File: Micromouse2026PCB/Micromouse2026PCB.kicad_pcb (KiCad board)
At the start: 2 copper layers, 12 parts, among them J1 Power Terminal, U6 L7805

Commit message: New PCB work
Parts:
- added J2: i2c OLED, Connector_PinHeader_2.54mm:PinHeader_1x04_P2.54mm_Vertical, F.Cu at (83.8, 54.0)
- added J3: BNO085, Connector_PinHeader_2.54mm:PinHeader_1x06_P2.54mm_Vertical, F.Cu at (83.8, 34.9)
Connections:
- A1 pad A4: unconnected-(A1-PadA4) -> Net-(M1-OB)
- A1 pad A5: unconnected-(A1-PadA5) -> Net-(M2-OB)
- A1 pad D0: unconnected-(A1-D0/RX-PadD0) -> Net-(A1-D0/RX)
- A1 pad D1: unconnected-(A1-D1/TX-PadD1) -> Net-(A1-D1/TX)
- A1 pad D10: unconnected-(A1-PadD10) -> Net-(MD2-OB)
- A1 pad D5: unconnected-(A1-PadD5) -> Net-(MD1-OA)
- A1 pad D6: unconnected-(A1-PadD6) -> Net-(MD1-OB)
- A1 pad D9: unconnected-(A1-PadD9) -> Net-(MD2-OA)
- M1 pad 1: unconnected-(M1-MA-Pad1) -> Net-(M1-MA)
- M1 pad 2: unconnected-(M1-MB-Pad2) -> Net-(M1-MB)
- M1 pad 3: unconnected-(M1-VCC-Pad3) -> +5V
- M1 pad 4: unconnected-(M1-GND-Pad4) -> GND
- M1 pad 5: unconnected-(M1-OA-Pad5) -> Net-(A1-D1/TX)
- M1 pad 6: unconnected-(M1-OB-Pad6) -> Net-(M1-OB)
- M2 pad 1: unconnected-(M2-MA-Pad1) -> Net-(M2-MA)
- M2 pad 2: unconnected-(M2-MB-Pad2) -> Net-(M2-MB)
- M2 pad 3: unconnected-(M2-VCC-Pad3) -> +5V
- M2 pad 4: unconnected-(M2-GND-Pad4) -> GND
- M2 pad 5: unconnected-(M2-OA-Pad5) -> Net-(A1-D0/RX)
- M2 pad 6: unconnected-(M2-OB-Pad6) -> Net-(M2-OB)
- MD1 pad 1: unconnected-(MD1-OA-Pad1) -> Net-(MD1-OA)
- MD1 pad 4: unconnected-(MD1-OB-Pad4) -> Net-(MD1-OB)
- MD1 pad 6: unconnected-(MD1-IA-Pad6) -> Net-(M1-MA)
- MD1 pad 7: unconnected-(MD1-IB-Pad7) -> Net-(M1-MB)
- MD2 pad 1: unconnected-(MD2-OA-Pad1) -> Net-(MD2-OA)
- MD2 pad 4: unconnected-(MD2-OB-Pad4) -> Net-(MD2-OB)
- MD2 pad 6: unconnected-(MD2-IA-Pad6) -> Net-(M2-MA)
- MD2 pad 7: unconnected-(MD2-IB-Pad7) -> Net-(M2-MB)
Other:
- board outline added: 87 x 48.9 mm

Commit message: finished schematic
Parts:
- added SW1: RotaryEncoder_Switch, Rotary_Encoder:RotaryEncoder_Alps_EC11E-Switch_Vertical_H20mm, F.Cu at (90.4, 39.5)
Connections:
- A1 pad D10: Net-(MD2-OB) -> Net-(MD2-IB)
- A1 pad D4: unconnected-(A1-PadD4) -> Net-(A1-PadD4)
- A1 pad D5: Net-(MD1-OA) -> Net-(MD1-IA)
- A1 pad D6: Net-(MD1-OB) -> Net-(MD1-IB)
- A1 pad D7: unconnected-(A1-D7_INT4-PadD7) -> Net-(A1-D7_INT4)
- A1 pad D8: unconnected-(A1-PadD8) -> Net-(A1-PadD8)
- A1 pad D9: Net-(MD2-OA) -> Net-(MD2-IA)
- MD1 pad 1: Net-(MD1-OA) -> Net-(M1-MA)
- MD1 pad 4: Net-(MD1-OB) -> Net-(M1-MB)
- MD1 pad 6: Net-(M1-MA) -> Net-(MD1-IA)
- MD1 pad 7: Net-(M1-MB) -> Net-(MD1-IB)
- MD2 pad 1: Net-(MD2-OA) -> Net-(M2-MA)
- MD2 pad 4: Net-(MD2-OB) -> Net-(M2-MB)
- MD2 pad 6: Net-(M2-MA) -> Net-(MD2-IA)
- MD2 pad 7: Net-(M2-MB) -> Net-(MD2-IB)
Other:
- board outline removed

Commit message: PCB work
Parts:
- J2: footprint Connector_PinHeader_2.54mm:PinHeader_1x04_P2.54mm_Vertical -> CustomFootprints:OLED_0.96_SSD1306_I2C
- J3: footprint Connector_PinHeader_2.54mm:PinHeader_1x06_P2.54mm_Vertical -> CustomFootprints:Adafruit_BNO085
- moved J3 54.1 mm to (137.2, 43.8)
- moved J2 42.1 mm to (125.7, 58.4)
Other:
- board outline added: 24.9 x 25.5 mm

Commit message: PCB working version
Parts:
- removed U6: L7805, Package_TO_SOT_THT:TO-220-3_Vertical
- added D1: 1N5822, Diode_THT:D_DO-201AD_P15.24mm_Horizontal, F.Cu at (123.2, 88.3)
- added R1: 10k, Resistor_THT:R_Axial_DIN0207_L6.3mm_D2.5mm_P10.16mm_Horizontal, F.Cu at (100.1, 87.6)
- added R2: 10k, Resistor_THT:R_Axial_DIN0207_L6.3mm_D2.5mm_P10.16mm_Horizontal, F.Cu at (104.1, 87.6)
- added SW1: PowerSW, Connector_PinHeader_2.54mm:PinHeader_1x03_P2.54mm_Vertical, F.Cu at (118.7, 81.3)
- J1: footprint TerminalBlock_Phoenix:TerminalBlock_Phoenix_MKDS-1,5-2-5.08_1x02_P5.08mm_Horizontal -> TerminalBlock_Phoenix:TerminalBlock_Phoenix_MPT-0,5-2-2.54_1x02_P2.54mm_Horizontal
- moved J3 94.1 mm to (43.2, 48.3), turned to 180 degrees
- moved J1 80.2 mm to (102.9, 71.1), turned to 180 degrees
- moved A1 49.2 mm to (70.0, 81.4), turned to 90 degrees
- moved M2 38.0 mm to (48.3, 35.6), turned to -90 degrees
- moved RS1 33.0 mm to (109.3, 66.6)
- moved J2 31.4 mm to (99.1, 41.9), turned to 90 degrees
- moved U1 29.9 mm to (30.5, 83.8), turned to 90 degrees
- moved MD2 29.6 mm to (43.2, 43.2), turned to 180 degrees
- moved MD1 28.8 mm to (35.6, 71.1)
- moved U4 27.3 mm to (29.3, 36.7), turned to -45 degrees
- moved U5 26.6 mm to (43.2, 30.5), turned to -90 degrees
- moved U3 25.4 mm to (20.3, 50.8)
- moved U2 24.9 mm to (20.3, 68.6), turned to 45 degrees
- moved M1 12.1 mm to (48.3, 71.1), turned to -90 degrees
- renumbered SW1 to RS1
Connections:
- A1 pad A4: Net-(M1-OB) -> unconnected-(A1-PadA4)
- A1 pad A5: Net-(M2-OB) -> Net-(A1-PadA5)
- A1 pad D11: unconnected-(A1-PadD11) -> Net-(M2-OB)
- A1 pad D12: unconnected-(A1-PadD12) -> Net-(M1-OB)
- A1 pad VIN: Net-(J1-Pin_1) -> Net-(SW1-Pin_1)
- J1 pad 1: Net-(J1-Pin_1) -> Net-(D1-A)
- MD1 pad 2: Net-(U6-OUT) -> Net-(SW1-Pin_1)
- MD1 pad 3: Net-(U6-OUT) -> Net-(SW1-Pin_1)
- MD2 pad 2: Net-(U6-OUT) -> Net-(SW1-Pin_1)
- MD2 pad 3: Net-(U6-OUT) -> Net-(SW1-Pin_1)
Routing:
- net GND: track 0.00 -> 513.9 mm
- net +5V: track 0.00 -> 313.3 mm
- net Net-(SW1-Pin_1): track 0.00 -> 271.6 mm
- net /SDA: track 0.00 -> 255.9 mm
- net /SCL: track 0.00 -> 243.8 mm
- net Net-(MD2-IB): track 0.00 -> 127.7 mm
- net Net-(A1-PadA5): track 0.00 -> 112.7 mm
- net Net-(A1-PadD4): track 0.00 -> 88.3 mm
- net Net-(M2-OB): track 0.00 -> 82.6 mm
- net Net-(U4-XSHUT): track 0.00 -> 79.7 mm, vias 0 -> 1
- net Net-(A1-PadD8): track 0.00 -> 73.1 mm
- net Net-(A1-D7_INT4): track 0.00 -> 69.8 mm
- net Net-(U3-XSHUT): track 0.00 -> 66.0 mm, vias 0 -> 1
- net Net-(MD2-IA): track 0.00 -> 62.9 mm
- net Net-(MD1-IA): track 0.00 -> 61.3 mm
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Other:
- board size 24.9 x 25.5 mm -> 109.2 x 68.6 mm

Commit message: polarity indicator
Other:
- board text added: "GND V+"
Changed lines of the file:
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@@
 		(layer "Edge.Cuts")
+	)
+	(gr_text "GND V+"
+		(at 95.25 67.31 0)
+		(layer "F.SilkS")
+		(effects
+			(font
+				(size 2 2)
+				(thickness 0.4)
+			)
+			(justify left bottom)
+		)
 	)
 	(segment

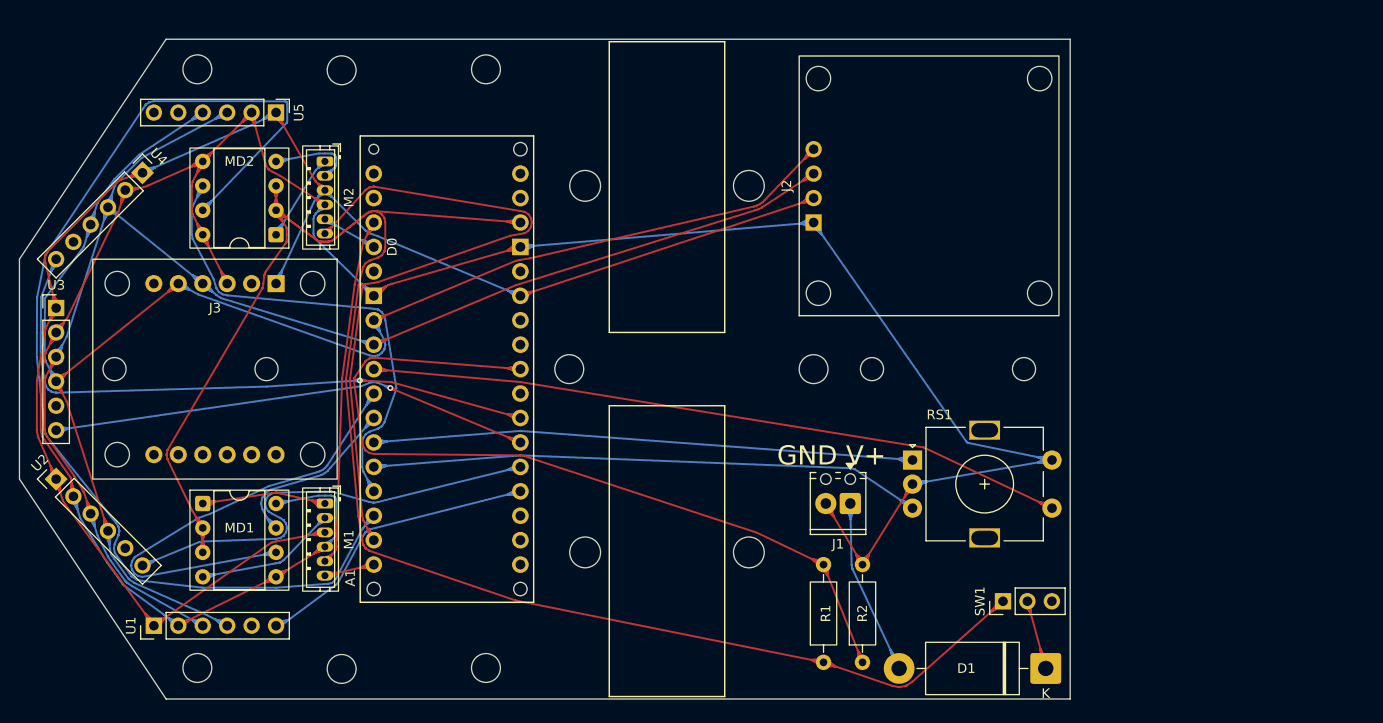
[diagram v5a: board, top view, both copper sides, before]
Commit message: Dual Castors
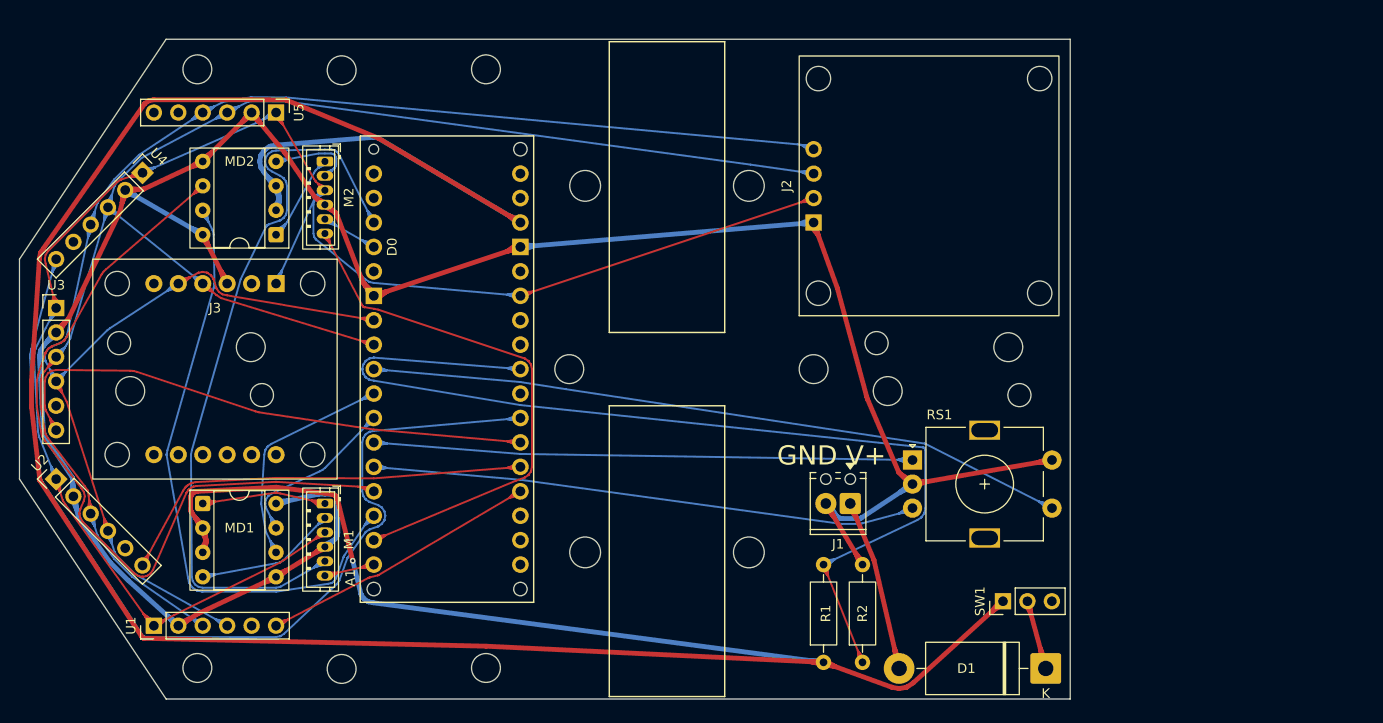
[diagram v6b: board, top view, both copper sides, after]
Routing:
- net GND: track 513.9 -> 347.3 mm
- net Net-(SW1-Pin_1): track 271.6 -> 350.2 mm, vias 0 -> 1
- net Net-(MD2-IB): track 127.7 -> 76.7 mm
- net Net-(A1-D1/TX): track 48.2 -> 92.5 mm
- net Net-(U4-XSHUT): track 79.7 -> 113.7 mm, vias 1 -> 0
- net Net-(MD2-IA): track 62.9 -> 95.3 mm
- net Net-(MD1-IA): track 61.3 -> 36.9 mm
- net Net-(A1-PadA5): track 112.7 -> 132.3 mm
- net Net-(M2-OB): track 82.6 -> 69.5 mm
- net /SCL: track 243.8 -> 256.4 mm
- net Net-(D1-K): track 28.5 -> 15.9 mm
- net Net-(D1-A): track 39.5 -> 27.6 mm
- net /SDA: track 255.9 -> 265.2 mm
- net +5V: track 313.3 -> 322.5 mm
- net Net-(U3-XSHUT): track 66.0 -> 69.9 mm, vias 1 -> 0
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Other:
- outline, holes or cut-outs redrawn

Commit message: PCB done
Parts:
- moved D1 26.5 mm to (104.1, 69.8), turned to -90 degrees
- moved J1 21.3 mm to (123.2, 64.8)
- moved R1 20.7 mm to (120.7, 85.1), turned to 180 degrees
- moved R2 8.98 mm to (113.0, 88.9), turned to 180 degrees
- moved SW1 8.26 mm to (121.9, 88.9), turned to -90 degrees
- moved RS1 6.47 mm to (109.2, 73.1)
- moved U5 1.27 mm to (44.5, 30.5)
- moved U1 1.27 mm to (31.8, 83.8)
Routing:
- net Net-(SW1-Pin_1): track 350.2 -> 0.00 mm, vias 1 -> 0
- net GND: track 347.3 -> 0.00 mm
- net +5V: track 322.5 -> 0.00 mm
- net /SDA: track 265.2 -> 0.00 mm
- net /SCL: track 256.4 -> 0.00 mm
- net Net-(A1-PadA5): track 132.3 -> 0.00 mm
- net Net-(U4-XSHUT): track 113.7 -> 0.00 mm
- net Net-(MD2-IA): track 95.3 -> 0.00 mm
- net Net-(A1-D1/TX): track 92.5 -> 0.00 mm
- net Net-(A1-PadD4): track 88.4 -> 0.00 mm
- net Net-(MD2-IB): track 76.7 -> 0.00 mm
- net Net-(A1-PadD8): track 71.1 -> 0.00 mm
- net Net-(U3-XSHUT): track 69.9 -> 0.00 mm
- net Net-(A1-D7_INT4): track 69.7 -> 0.00 mm
- net Net-(M2-OB): track 69.5 -> 0.00 mm
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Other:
- outline, holes or cut-outs redrawn
- board text added: "M1"
- board text added: "M2"

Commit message: Actually really done this time
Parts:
- moved D1 62.7 mm to (53.3, 33.0), turned to 0 degrees
- moved J1 21.8 mm to (105.4, 77.5)
- moved A1 3.41 mm to (70.0, 84.8)
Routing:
- net GND: track 0.00 -> 459.0 mm
- net +5V: track 0.00 -> 346.7 mm
- net /SDA: track 0.00 -> 276.6 mm
- net /SCL: track 0.00 -> 250.1 mm
- net Net-(SW1-Pin_1): track 0.00 -> 209.4 mm, vias 0 -> 3
- net Net-(D1-K): track 0.00 -> 103.4 mm
- net Net-(U4-XSHUT): track 0.00 -> 99.4 mm, vias 0 -> 1
- net Net-(M2-OB): track 0.00 -> 89.6 mm
- net Net-(MD2-IB): track 0.00 -> 88.8 mm, vias 0 -> 2
- net Net-(A1-PadD4): track 0.00 -> 88.8 mm
- net Net-(A1-D1/TX): track 0.00 -> 81.2 mm
- net Net-(A1-PadA5): track 0.00 -> 80.1 mm
- net Net-(A1-PadD8): track 0.00 -> 76.0 mm, vias 0 -> 1
- net Net-(D1-A): track 0.00 -> 70.5 mm
- net Net-(A1-D7_INT4): track 0.00 -> 69.9 mm
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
